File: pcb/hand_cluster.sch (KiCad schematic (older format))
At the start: 65 parts, among them J1 AudioJack4, J2 AudioJack4, U1 ProMicro

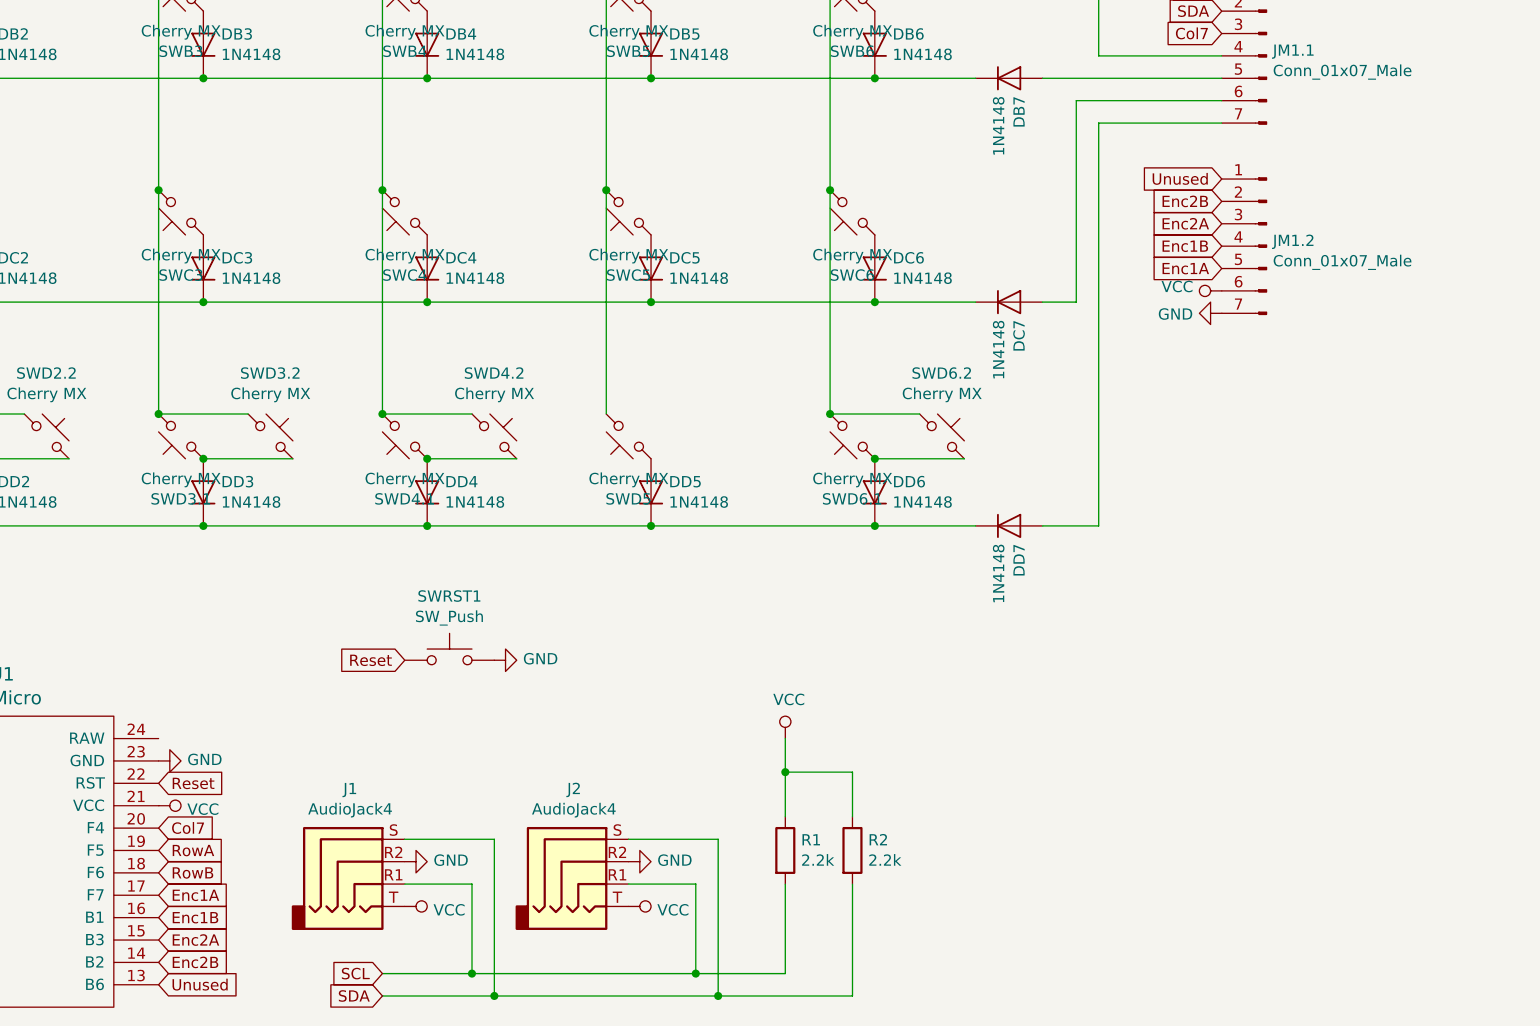
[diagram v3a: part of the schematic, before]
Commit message: Modified the main pcb hand cluster to a near completed prototype design
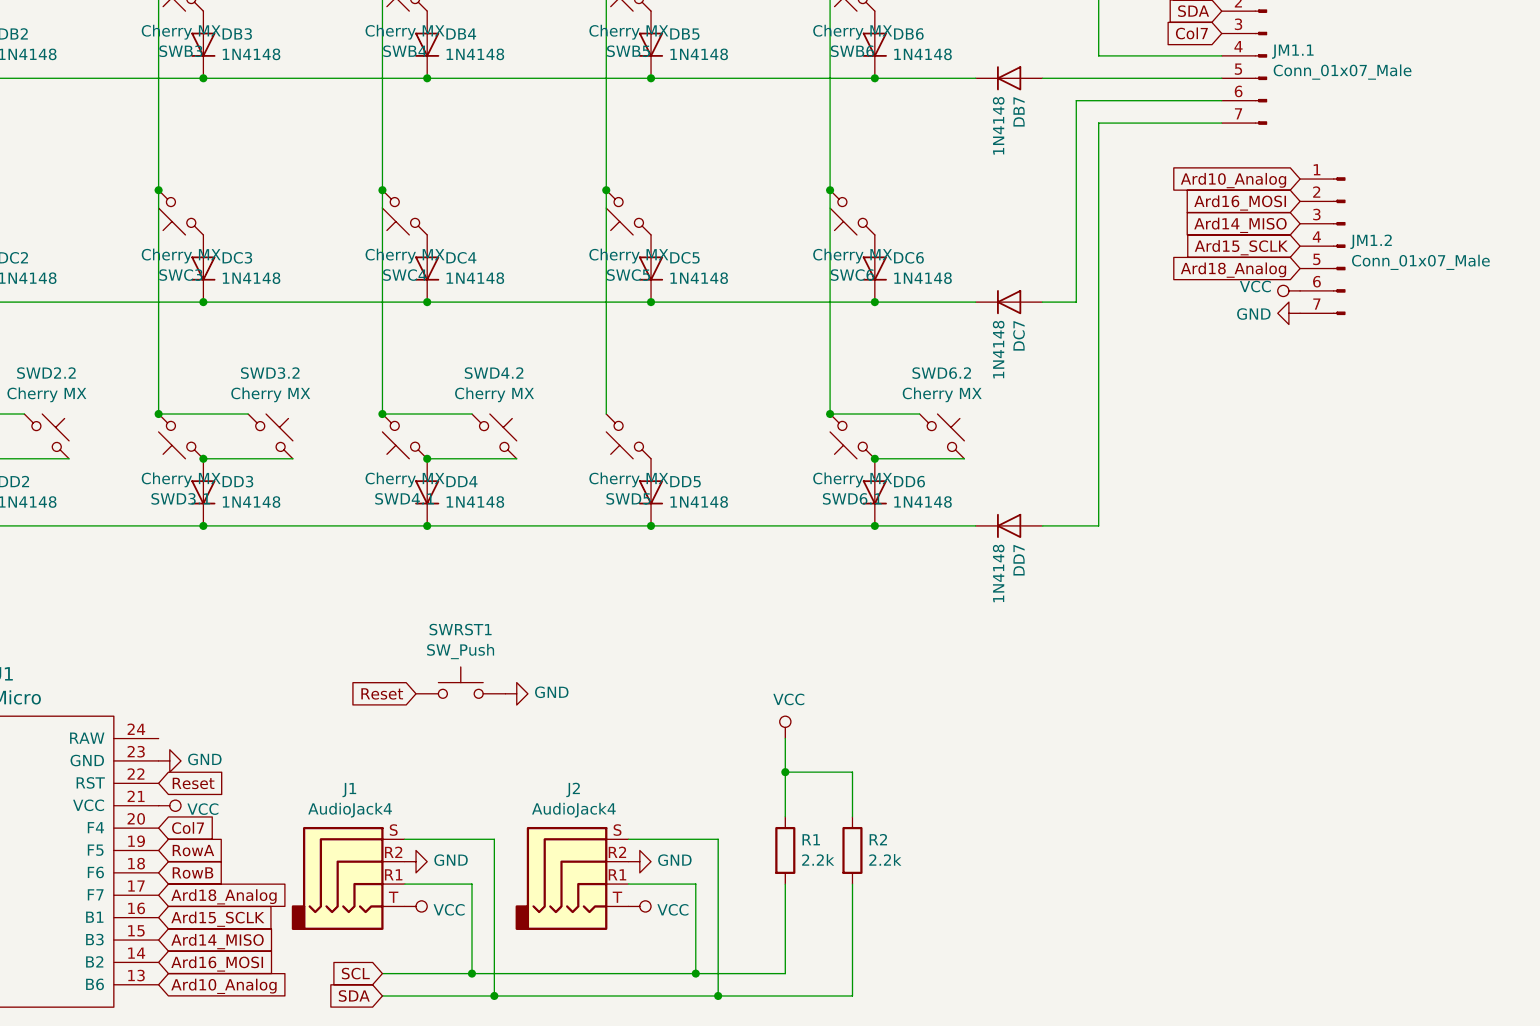
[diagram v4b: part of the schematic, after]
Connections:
- net Enc1A renamed Ard18_Analog
- net Enc1B renamed Ard15_SCLK
- net Enc2A renamed Ard14_MISO
- net Enc2B renamed Ard16_MOSI
- net Unused renamed Ard10_Analog
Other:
- moved on the sheet: JM1.2, SWRST1
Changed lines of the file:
@@
 Text GLabel 2100 6550 0    50   Input ~ 0
 Col6
-Text GLabel 3500 6750 2    50   Input ~ 0
-Enc1B
-Text GLabel 3500 6650 2    50   Input ~ 0
-Enc1A
 Text GLabel 2100 6450 0    50   Input ~ 0
 SDA
@@
 Wire Wire Line
 	6700 4700 7100 4700
-Text GLabel 8250 3850 0    50   Input ~ 0
-Enc1A
-Text GLabel 8250 3750 0    50   Input ~ 0
-Enc1B
-Text GLabel 8250 3650 0    50   Input ~ 0
-Enc2A
-Text GLabel 8250 3550 0    50   Input ~ 0
-Enc2B
 Text GLabel 7500 1000 1    50   Input ~ 0
 Col7
@@
 	7500 1500 7850 1500
 Connection ~ 7500 1500
-$Comp
-L power:GND #PWR0106
-U 1 1 5D95D59E
-P 8250 4050
-F 0 "#PWR0106" H 8250 3800 50  0001 C CNN
-F 1 "GND" V 8255 3922 50  0000 R CNN
-F 2 "" H 8250 4050 50  0001 C CNN
-F 3 "" H 8250 4050 50  0001 C CNN
-	1    8250 4050
-	0    1    1    0
-$EndComp
-$Comp
-L power:VCC #PWR0105
-U 1 1 5D95C408
-P 8250 3950
-F 0 "#PWR0105" H 8250 3800 50  0001 C CNN
-F 1 "VCC" V 8268 4077 50  0000 L CNN
-F 2 "" H 8250 3950 50  0001 C CNN
-F 3 "" H 8250 3950 50  0001 C CNN
-	1    8250 3950
-	0    -1   -1   0
-$EndComp
 Text GLabel 8250 2600 0    50   Input ~ 0
 SCL
@@
 Col1
 $Comp
-L Connector:Conn_01x07_Male JM1.2
-U 1 1 5D99061A
-P 8450 3750
-F 0 "JM1.2" H 8422 3774 50  0000 R CNN
-F 1 "Conn_01x07_Male" H 8422 3683 50  0000 R CNN
-F 2 "Connector_PinHeader_2.54mm:PinHeader_1x07_P2.54mm_Vertical" H 8450 3750 50  0001 C CNN
-F 3 "~" H 8450 3750 50  0001 C CNN
-	1    8450 3750
-	-1   0    0    -1
-$EndComp
-$Comp
 L Connector:Conn_01x07_Male JM1.1
 U 1 1 5D993DAB
@@
 Text GLabel 2100 6750 0    50   Input ~ 0
 Col4
-Text GLabel 8250 3450 0    50   Input ~ 0
-Unused
 Wire Wire Line
 	7450 2000 7700 2000
@@
 Wire Wire Line
 	1500 1500 1500 2500
-Text GLabel 4600 5600 0    50   Input ~ 0
+Text GLabel 4650 5750 0    50   Input ~ 0
 Reset
 $Comp
 L Switch:SW_Push SWRST1
 U 1 1 5DB5FDC2
-P 4800 5600
-F 0 "SWRST1" H 4800 5885 50  0000 C CNN
-F 1 "SW_Push" H 4800 5794 50  0000 C CNN
-F 2 "Button_Switch_THT:SW_PUSH_6mm" H 4800 5800 50  0001 C CNN
-F 3 "~" H 4800 5800 50  0001 C CNN
-	1    4800 5600
+P 4850 5750
+F 0 "SWRST1" H 4850 6035 50  0000 C CNN
+F 1 "SW_Push" H 4850 5944 50  0000 C CNN
+F 2 "Button_Switch_THT:SW_PUSH_6mm" H 4850 5950 50  0001 C CNN
+F 3 "~" H 4850 5950 50  0001 C CNN
+	1    4850 5750
 	1    0    0    -1
 $EndComp
@@
 L power:GND #PWR0111
 U 1 1 5DB68E40
-P 5000 5600
-F 0 "#PWR0111" H 5000 5350 50  0001 C CNN
-F 1 "GND" V 5005 5472 50  0000 R CNN
-F 2 "" H 5000 5600 50  0001 C CNN
-F 3 "" H 5000 5600 50  0001 C CNN
-	1    5000 5600
+P 5050 5750
+F 0 "#PWR0111" H 5050 5500 50  0001 C CNN
+F 1 "GND" V 5055 5622 50  0000 R CNN
+F 2 "" H 5050 5750 50  0001 C CNN
+F 3 "" H 5050 5750 50  0001 C CNN
+	1    5050 5750
 	0    -1   -1   0
 $EndComp
@@
 Text GLabel 2100 6950 0    50   Input ~ 0
 Col2
-Text GLabel 3500 6950 2    50   Input ~ 0
-Enc2B
-Text GLabel 3500 6850 2    50   Input ~ 0
-Enc2A
-Text GLabel 3500 7050 2    50   Input ~ 0
-Unused
 Text GLabel 3500 6550 2    50   Input ~ 0
 RowB
@@
 Wire Wire Line
 	6000 7100 6600 7100
+Text GLabel 3500 6950 2    50   Input ~ 0
+Ard16_MOSI
+Text GLabel 3500 7050 2    50   Input ~ 0
+Ard10_Analog
+Text GLabel 3500 6850 2    50   Input ~ 0
+Ard14_MISO
+Text GLabel 3500 6750 2    50   Input ~ 0
+Ard15_SCLK
+Text GLabel 3500 6650 2    50   Input ~ 0
+Ard18_Analog
+$Comp
+L power:GND #PWR0106
+U 1 1 5D95D59E
+P 8600 4050
+F 0 "#PWR0106" H 8600 3800 50  0001 C CNN
+F 1 "GND" V 8605 3922 50  0000 R CNN
+F 2 "" H 8600 4050 50  0001 C CNN
+F 3 "" H 8600 4050 50  0001 C CNN
+	1    8600 4050
+	0    1    1    0
+$EndComp
+$Comp
+L power:VCC #PWR0105
+U 1 1 5D95C408
+P 8600 3950
+F 0 "#PWR0105" H 8600 3800 50  0001 C CNN
+F 1 "VCC" V 8618 4077 50  0000 L CNN
+F 2 "" H 8600 3950 50  0001 C CNN
+F 3 "" H 8600 3950 50  0001 C CNN
+	1    8600 3950
+	0    -1   -1   0
+$EndComp
+$Comp
+L Connector:Conn_01x07_Male JM1.2
+U 1 1 5D99061A
+P 8800 3750
+F 0 "JM1.2" H 8772 3774 50  0000 R CNN
+F 1 "Conn_01x07_Male" H 8772 3683 50  0000 R CNN
+F 2 "Connector_PinHeader_2.54mm:PinHeader_1x07_P2.54mm_Vertical" H 8800 3750 50  0001 C CNN
+F 3 "~" H 8800 3750 50  0001 C CNN
+	1    8800 3750
+	-1   0    0    -1
+$EndComp
+Text GLabel 8600 3450 0    50   Input ~ 0
+Ard10_Analog
+Text GLabel 8600 3550 0    50   Input ~ 0
+Ard16_MOSI
+Text GLabel 8600 3650 0    50   Input ~ 0
+Ard14_MISO
+Text GLabel 8600 3750 0    50   Input ~ 0
+Ard15_SCLK
+Text GLabel 8600 3850 0    50   Input ~ 0
+Ard18_Analog
 $EndSCHEMATC
